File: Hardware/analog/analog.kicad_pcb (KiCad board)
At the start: 4 copper layers, 128 x 182 mm, 79 parts, among them J201 Würth 74651194R, J202 Würth 74651194R, J301 Conn_02x10_Odd_Even, M501 Fan_4pin, Q201 IXTH80N075L2, Q501 MMBT3904, U201 ADA4522-2, U202 LM431SC, U301 ADUM131D, U302 ADUM131D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

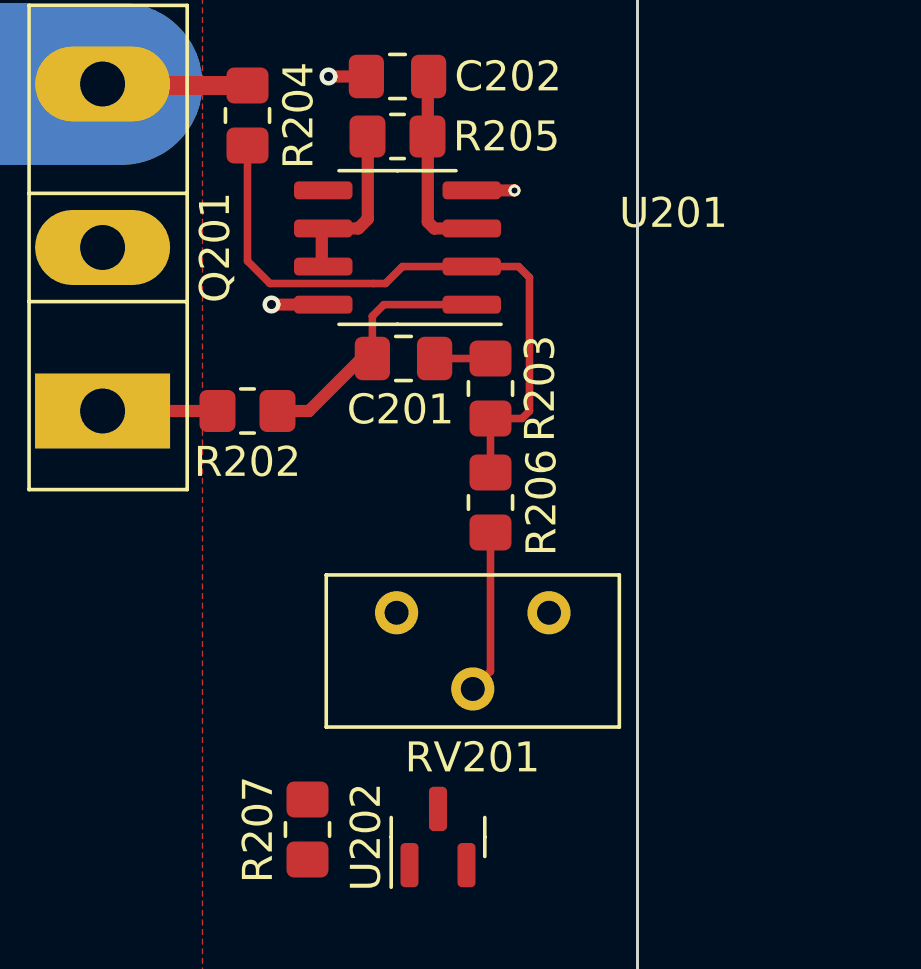
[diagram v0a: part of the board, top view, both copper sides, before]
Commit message: Minor analog board layout tweaks
- Mostly to do with the last of the analog bits for the first channel
  (reisstors and capacitors, as well as the zero offset trimmer)
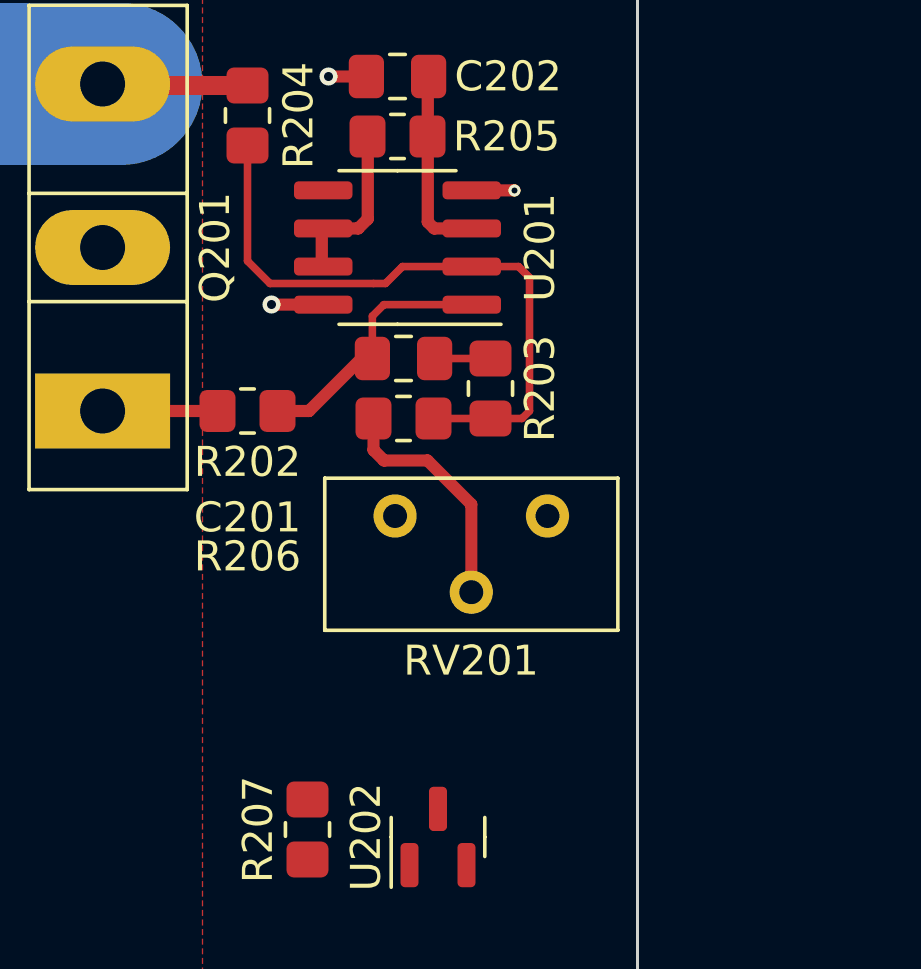
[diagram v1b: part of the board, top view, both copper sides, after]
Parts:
- moved R206 4.03 mm to (122.2, 85.8), turned to 0 degrees
- moved RV201 3.23 mm to (127.0, 89.0)
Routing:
- net Net-(R206-Pad1): track 5.46 -> 7.99 mm
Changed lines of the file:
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@@
     (property "Sheetname" "MOSFET Load")
     (attr smd)
-    (fp_text reference "C201" (at -0.1 1.7) (layer "F.SilkS")
+    (fp_text reference "C201" (at -5.2 5.3) (layer "F.SilkS")
       (effects (font (size 1 1) (thickness 0.15)))
     )
@@
   )
   (footprint "programmable-load:Potentiometer_Nidec_Copal_CT94EY" (layer "F.Cu")
-    (at 127.05 92.225)
+    (at 127 89)
     (descr "Potentiometer, vertical, Nidec-Copal CT-94EY (Vertical)")
     (tags "Potentiometer vertical nidec ct94")
@@
   )
   (footprint "Resistor_SMD:R_0805_2012Metric_Pad1.20x1.40mm_HandSolder" (layer "F.Cu")
-    (at 125.1 88.55 90)
+    (at 122.2 85.75)
     (descr "Resistor SMD 0805 (2012 Metric), square (rectangular) end terminal, IPC_7351 nominal with elongated pad for handsoldering. (Body size source: IPC-SM-782 page 72, https://www.pcb-3d.com/wordpress/wp-content/uploads/ipc-sm-782a_amendment_1_and_2.pdf), generated with kicad-footprint-generator")
     (tags "resistor handsolder")
@@
     (property "Sheetname" "MOSFET Load")
     (attr smd)
-    (fp_text reference "R206" (at 0 1.7 90) (layer "F.SilkS")
+    (fp_text reference "R206" (at -5.2 4.6) (layer "F.SilkS")
       (effects (font (size 1 1) (thickness 0.15)))
     )
-    (fp_text value "330k (?)" (at 0 1.65 90) (layer "F.Fab") hide
+    (fp_text value "330k (?)" (at 0 1.65) (layer "F.Fab") hide
       (effects (font (size 1 1) (thickness 0.15)))
     )
-    (fp_text user "${REFERENCE}" (at 0 0 90) (layer "F.Fab")
+    (fp_text user "${REFERENCE}" (at 0 0) (layer "F.Fab")
       (effects (font (size 0.5 0.5) (thickness 0.08)))
     )
@@
     (fp_line (start 1 -0.625) (end 1 0.625) (layer "F.Fab") (width 0.1))
     (fp_line (start -1 0.625) (end -1 -0.625) (layer "F.Fab") (width 0.1))
-    (pad "1" smd roundrect (at -1 0 90) (size 1.2 1.4) (layers "F.Cu" "F.Paste" "F.Mask") (roundrect_rratio 0.208333)
+    (pad "1" smd roundrect (at -1 0) (size 1.2 1.4) (layers "F.Cu" "F.Paste" "F.Mask") (roundrect_rratio 0.208333)
       (net 71 "Net-(R206-Pad1)") (pintype "passive"))
-    (pad "2" smd roundrect (at 1 0 90) (size 1.2 1.4) (layers "F.Cu" "F.Paste" "F.Mask") (roundrect_rratio 0.208333)
+    (pad "2" smd roundrect (at 1 0) (size 1.2 1.4) (layers "F.Cu" "F.Paste" "F.Mask") (roundrect_rratio 0.208333)
       (net 69 "Net-(R203-Pad2)") (pintype "passive"))
     (model "${KICAD6_3DMODEL_DIR}/Resistor_SMD.3dshapes/R_0805_2012Metric.wrl"
@@
     (property "Sheetname" "MOSFET Load")
     (attr smd)
-    (fp_text reference "U201" (at -9.2 1.15 180) (layer "F.SilkS")
+    (fp_text reference "U201" (at -4.75 0 270) (layer "F.SilkS")
       (effects (font (size 1 1) (thickness 0.15)))
     )
@@
   (segment (start 123.0075 74.5) (end 123.0075 79.2) (width 0.4064) (layer "F.Cu") (net 67))
   (segment (start 116 85.5) (end 112.17 85.5) (width 0.4064) (layer "F.Cu") (net 68))
-  (segment (start 125.1 87.55) (end 125.1 85.75) (width 0.254) (layer "F.Cu") (net 69))
-  (segment (start 126.15 85.75) (end 125.1 85.75) (width 0.254) (layer "F.Cu") (net 69))
   (segment (start 126.4 81.05) (end 126.4 85.5) (width 0.254) (layer "F.Cu") (net 69))
+  (segment (start 124.475 80.685) (end 126.035 80.685) (width 0.254) (layer "F.Cu") (net 69))
   (segment (start 126.035 80.685) (end 126.4 81.05) (width 0.254) (layer "F.Cu") (net 69))
+  (segment (start 126.15 85.75) (end 123.2 85.75) (width 0.254) (layer "F.Cu") (net 69))
+  (segment (start 126.4 85.5) (end 126.15 85.75) (width 0.254) (layer "F.Cu") (net 69))
   (segment (start 122.165 80.685) (end 124.475 80.685) (width 0.254) (layer "F.Cu") (net 69))
   (segment (start 121.2 81.25) (end 121.6 81.25) (width 0.254) (layer "F.Cu") (net 69))
-  (segment (start 126.4 85.5) (end 126.15 85.75) (width 0.254) (layer "F.Cu") (net 69))
   (segment (start 117 76.65) (end 117 80.5) (width 0.254) (layer "F.Cu") (net 69))
-  (segment (start 124.475 80.685) (end 126.035 80.685) (width 0.254) (layer "F.Cu") (net 69))
   (segment (start 121.6 81.25) (end 122.165 80.685) (width 0.254) (layer "F.Cu") (net 69))
   (segment (start 117 80.5) (end 117.75 81.25) (width 0.254) (layer "F.Cu") (net 69))
@@
   (segment (start 120.6925 79.415) (end 121.0075 79.1) (width 0.4064) (layer "F.Cu") (net 70))
   (segment (start 119.475 80.685) (end 119.475 79.415) (width 0.4064) (layer "F.Cu") (net 70))
-  (segment (start 125.1 89.55) (end 125.1 94.175) (width 0.254) (layer "F.Cu") (net 71))
-  (segment (start 125.1 94.175) (end 124.51 94.765) (width 0.254) (layer "F.Cu") (net 71))
+  (segment (start 123 87.15) (end 121.55 87.15) (width 0.4064) (layer "F.Cu") (net 71))
+  (segment (start 121.55 87.15) (end 121.2 86.8) (width 0.4064) (layer "F.Cu") (net 71))
+  (segment (start 124.46 91.54) (end 124.46 88.61) (width 0.4064) (layer "F.Cu") (net 71))
+  (segment (start 121.2 86.8) (end 121.2 85.75) (width 0.4064) (layer "F.Cu") (net 71))
+  (segment (start 124.46 88.61) (end 123 87.15) (width 0.4064) (layer "F.Cu") (net 71))
   (zone (net 36) (net_name "GNDPWR") (layer "F.Cu") (hatch edge 0.508)
     (connect_pads (clearance 1.5))

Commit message: More tweaks to load board
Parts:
- added C312: 100nF, Capacitor_SMD:C_0805_2012Metric_Pad1.18x1.45mm_HandSolder, F.Cu at (4.90, 105.5)
- added G***: LOGO, LOGO, B.Cu at (27.4, 28.6)
- added J501: Conn_01x01, programmable-load:MillMax-2108-2, F.Cu at (42.5, 100.5)
- added J502: Conn_01x01, programmable-load:MillMax-2108-2, F.Cu at (45.0, 100.5)
- added JP301: Cfg WP, Connector_PinHeader_2.54mm:PinHeader_1x03_P2.54mm_Vertical, F.Cu at (0.17, 99.8)
- added U305: AT24CS32-SSHM, Package_SO:SOIC-8_3.9x4.9mm_P1.27mm, F.Cu at (6.72, 100.7)
- R207: value 2k2 -> 1k
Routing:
- net /Fan Control & Temperature Sensors/TEMP_DN: track 0.00 -> 7.76 mm
- net /Fan Control & Temperature Sensors/TEMP_DP: track 0.00 -> 6.10 mm

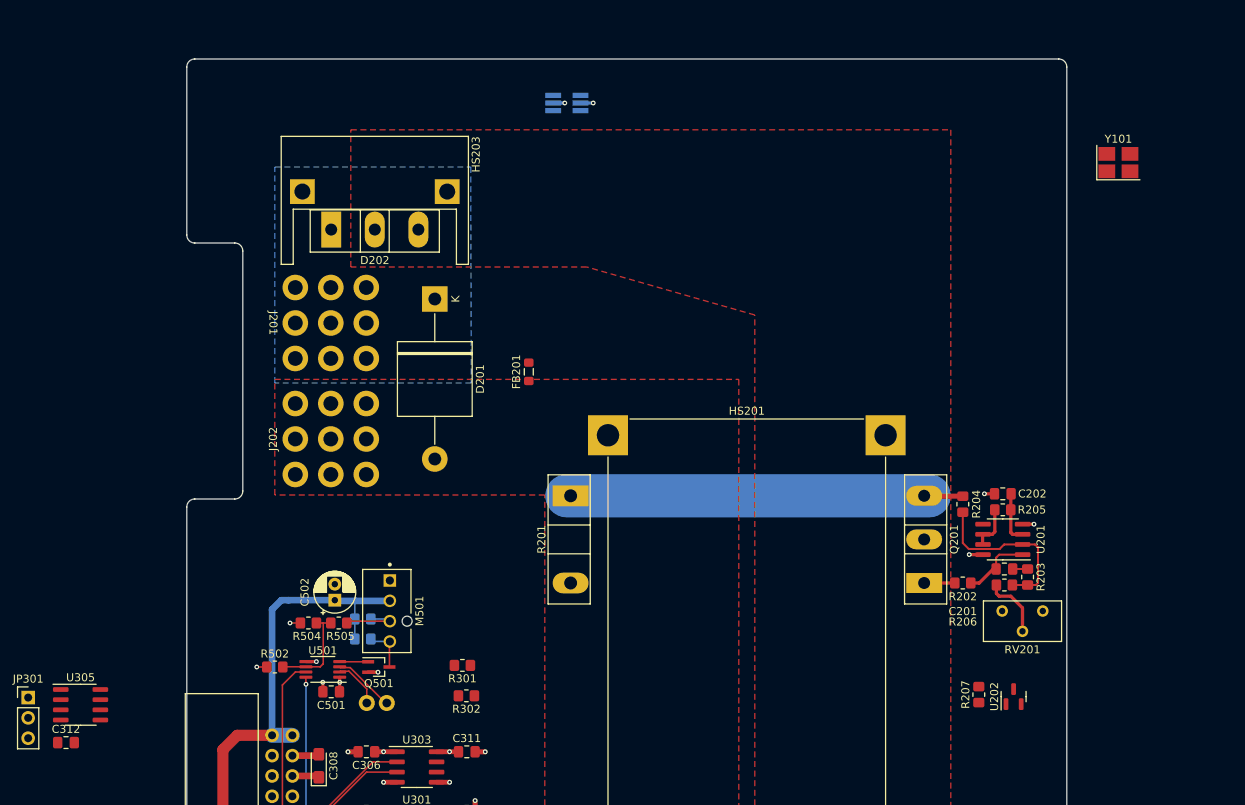
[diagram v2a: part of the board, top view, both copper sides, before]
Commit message: Added ADC/DAC section
- Imported the schematic for the analog DAC/ADC section, as well as the
  Vref generator and clock generator for the ADC
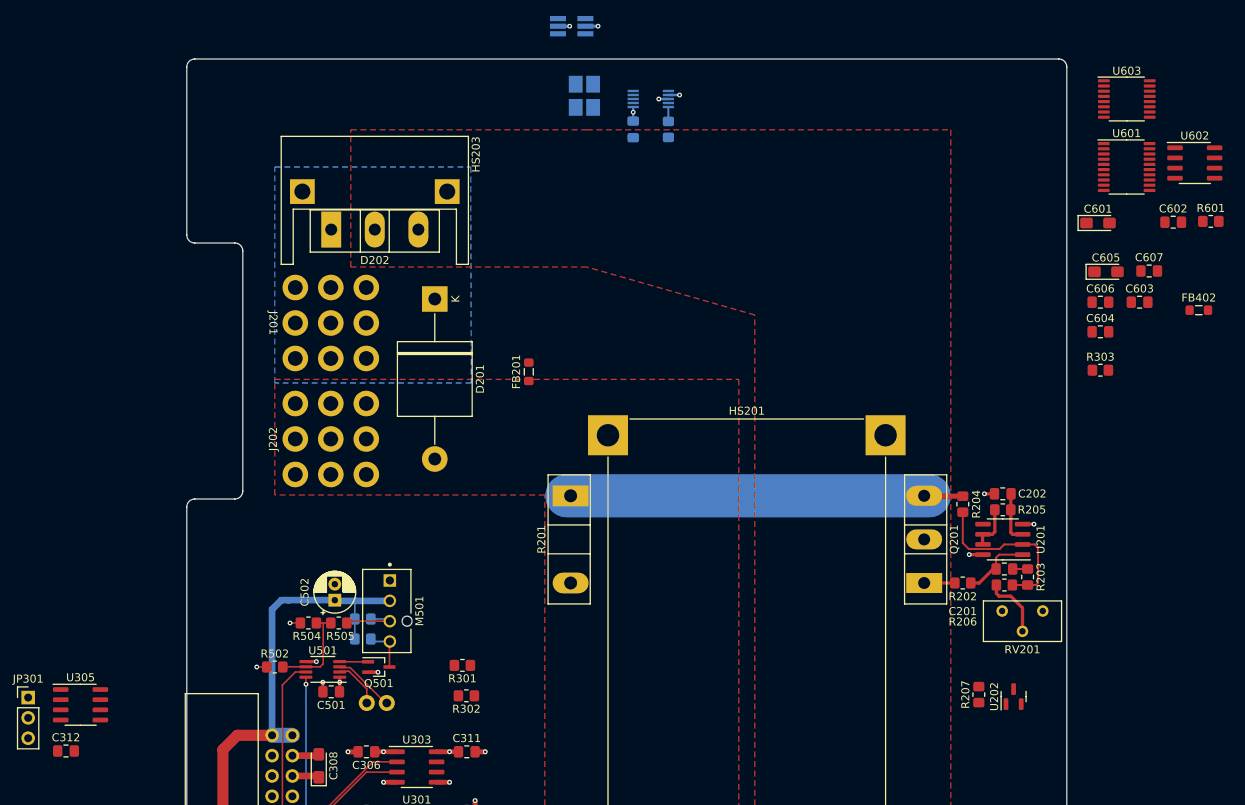
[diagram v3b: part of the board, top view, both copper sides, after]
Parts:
- removed Y101: 25MHz, Crystal:Crystal_SMD_SeikoEpson_TSX3225-4Pin_3.2x2.5mm_HandSoldering
- added C601: 10µF, Capacitor_Tantalum_SMD:CP_EIA-3216-18_Kemet-A_Pad1.58x1.35mm_HandSolder, F.Cu at (133.9, 40.5)
- added C602: 4.7µF, Capacitor_SMD:C_0805_2012Metric_Pad1.18x1.45mm_HandSolder, F.Cu at (143.3, 40.4)
- added C603: 100nF, Capacitor_SMD:C_0805_2012Metric_Pad1.18x1.45mm_HandSolder, F.Cu at (139.1, 50.4)
- added C604: 100nF, Capacitor_SMD:C_0805_2012Metric_Pad1.18x1.45mm_HandSolder, F.Cu at (134.2, 54.1)
- added C605: 10µF, Capacitor_Tantalum_SMD:CP_EIA-3216-18_Kemet-A_Pad1.58x1.35mm_HandSolder, F.Cu at (134.9, 46.6)
- added C606: 4.7µF, Capacitor_SMD:C_0805_2012Metric_Pad1.18x1.45mm_HandSolder, F.Cu at (134.2, 50.4)
- added C607: 100nF, Capacitor_SMD:C_0805_2012Metric_Pad1.18x1.45mm_HandSolder, F.Cu at (140.3, 46.5)
- added C701: 100nF, Capacitor_SMD:C_0805_2012Metric_Pad1.18x1.45mm_HandSolder, B.Cu at (75.8, 28.8)
- added FB402: FerriteBead_Small, Inductor_SMD:L_0805_2012Metric_Pad1.05x1.20mm_HandSolder, F.Cu at (146.5, 51.4)
- added R303: 10k, Resistor_SMD:R_0805_2012Metric_Pad1.20x1.40mm_HandSolder, F.Cu at (134.2, 58.9)
- added R601: 10k, Resistor_SMD:R_0805_2012Metric_Pad1.20x1.40mm_HandSolder, F.Cu at (148.0, 40.3)
- added R701: 0R, Resistor_SMD:R_0805_2012Metric_Pad1.20x1.40mm_HandSolder, B.Cu at (80.2, 28.8)
- added U601: MCP3564, Package_SO:TSSOP-20_4.4x6.5mm_P0.65mm, F.Cu at (137.5, 33.5)
- added U602: MAX6166, Package_SO:SOIC-8_3.9x4.9mm_P1.27mm, F.Cu at (146.0, 33.0)
- added U603: DAC8564, Package_SO:TSSOP-16_4.4x5mm_P0.65mm, F.Cu at (137.5, 25.0)
- added U701: Si5351A-B-GT, Package_SO:MSOP-10_3x3mm_P0.5mm, B.Cu at (78.0, 25.0)
- added Y701: 25MHz, Crystal:Crystal_SMD_SeikoEpson_TSX3225-4Pin_3.2x2.5mm_HandSoldering, B.Cu at (69.7, 24.6)
- moved U304 9.62 mm to (68.1, 15.9)
- moved C312 1.05 mm to (4.90, 106.5)
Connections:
- U301 pad 12: /External Interface/SPI_MISO -> /Analog stuff/SPI_MISO
- U301 pad 13: /External Interface/SPI_MOSI -> /Analog stuff/SPI_MOSI
- U301 pad 14: /External Interface/SPI_SCK -> /Analog stuff/SPI_SCK
- U302 pad 12: /External Interface/~{IRQ} -> /Analog stuff/~{IRQ}
- U304 pad 4: /External Interface/~{CS_DAC} -> /Analog stuff/~{CS_DAC}
- U304 pad 6: /External Interface/~{CS_ADC} -> /Analog stuff/~{CS_ADC}
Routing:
- net +3V3: track 19.4 -> 22.6 mm, vias 8 -> 10
- net Net-(U701-Pad10): track 0.00 -> 1.80 mm
- net GND: track 57.7 -> 58.9 mm, vias 67 -> 68
